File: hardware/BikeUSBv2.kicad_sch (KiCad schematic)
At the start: 52 parts, among them J1 TYPE-C-31-M-16, J2 JST S2B-EH(LF)(SN), SW1 1TS002E-2500-2501-CT, SW2 1TS002E-2500-2501-CT, U1 TPS63020DSJR, U2 ATtiny1616-M, U3 FUSB302B10MPX, U4 HT7550-2, U5 TPS25200

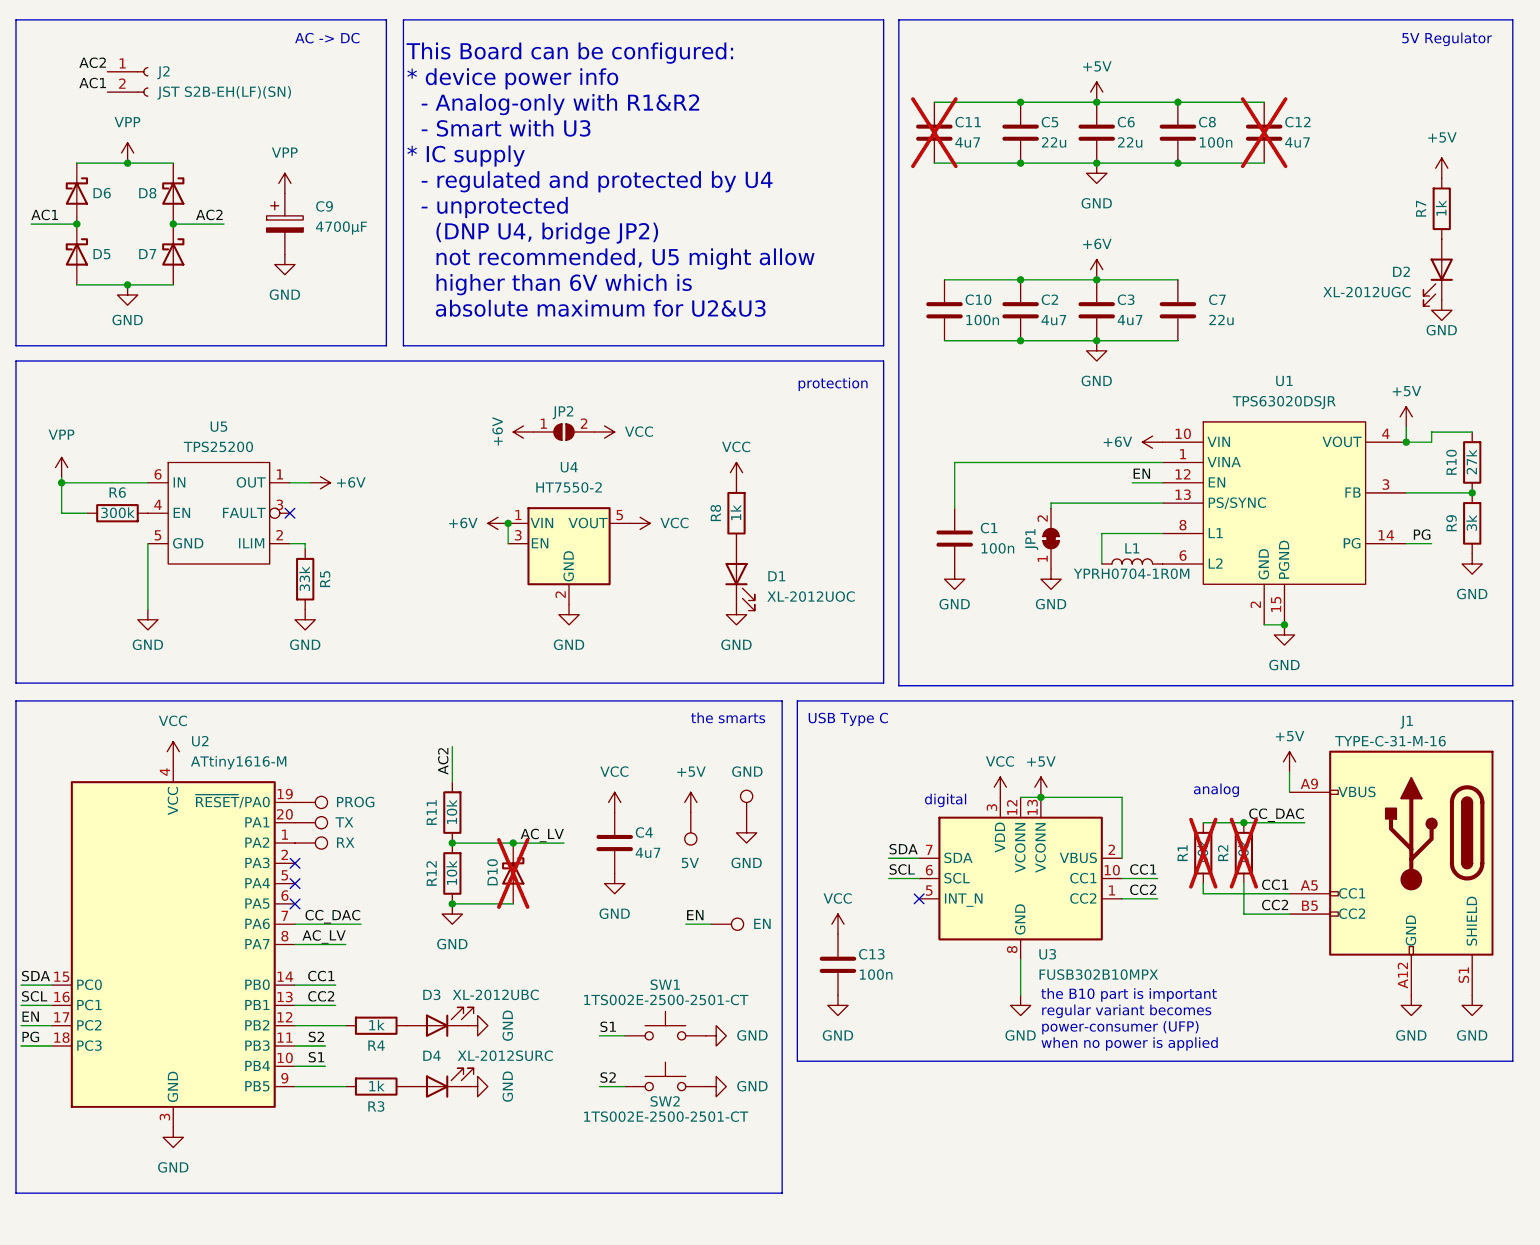
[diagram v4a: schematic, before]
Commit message: make U4 optional since new U5 clamps to 5V5
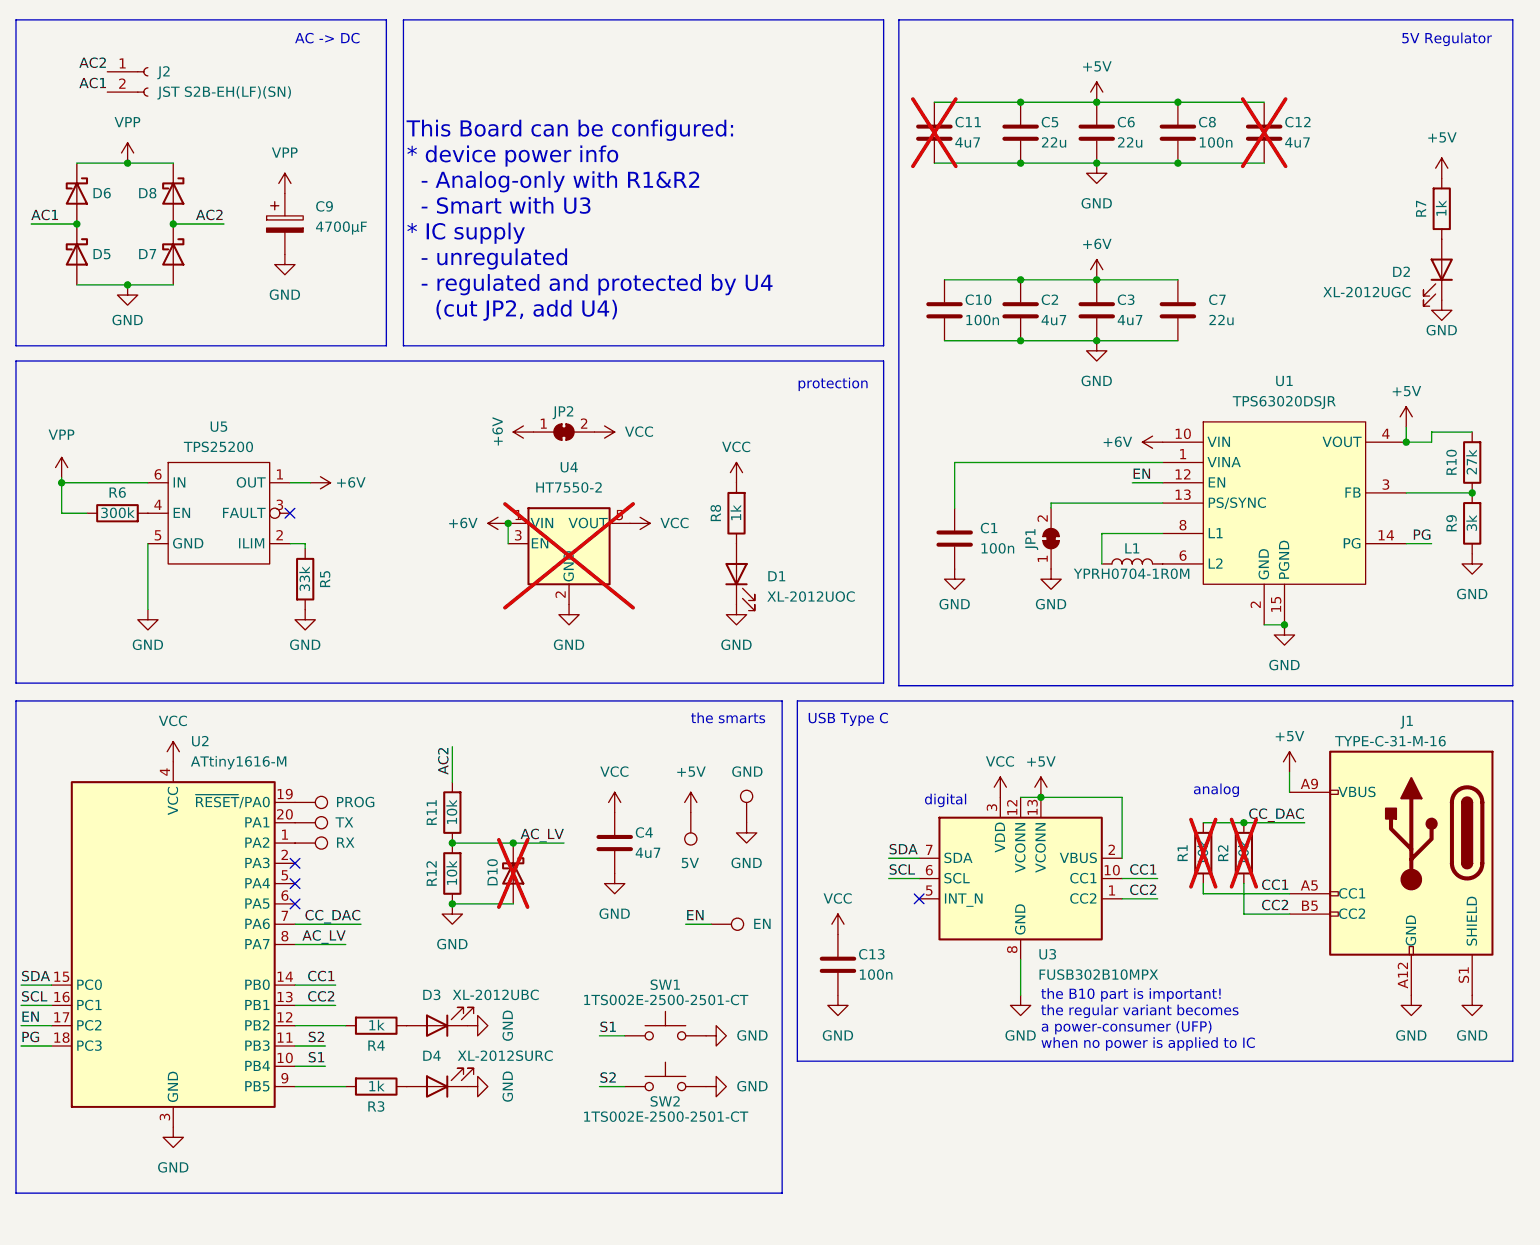
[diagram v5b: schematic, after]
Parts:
- JP2: footprint Jumper:SolderJumper-2_P1.3mm_Open_RoundedPad1.0x1.5mm -> Jumper:SolderJumper-2_P1.3mm_Bridged_RoundedPad1.0x1.5mm; symbol Jumper:SolderJumper_2_Open -> Jumper:SolderJumper_2_Bridged
- U4: now not fitted; now left out of the parts list
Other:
- note added: "This Board can be configured: * device power info - Analog-only with R1&R2 - Smart with U3 * IC supply - unregulated - regulated and protected by U4 (cut JP2, add U4)"
- note added: "the B10 part is important! the regular variant becomes a power-consumer (UFP) when no power is applied to IC"
- note removed: "This Board can be configured: * device power info - Analog-only with R1&R2 - Smart with U3 * IC supply - regulated and protected by U4 - unprotected (DNP U4, bridge JP2) not recommended, U5 might allow higher than 6V which is absolute maximum for U2&U3"
- note removed: "the B10 part is important regular variant becomes power-consumer (UFP) when no power is applied"
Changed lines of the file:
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@@
     (effects (font (size 1.27 1.27)) (justify left bottom))
   )
-  (text "the B10 part is important\nregular variant becomes\npower-consumer (UFP)\nwhen no power is applied"
+  (text "the B10 part is important!\nthe regular variant becomes\na power-consumer (UFP)\nwhen no power is applied to IC"
     (at 144.78 146.05 0)
     (effects (font (size 1.27 1.27)) (justify left bottom))
@@
     (effects (font (size 1.27 1.27)) (justify left bottom))
   )
-  (text "This Board can be configured:\n* device power info\n  - Analog-only with R1&R2\n  - Smart with U3\n* IC supply\n  - regulated and protected by U4\n  - unprotected\n    (DNP U4, bridge JP2)\n    not recommended, U5 might allow\n    higher than 6V which is\n    absolute maximum for U2&U3"
+  (text "This Board can be configured:\n* device power info\n  - Analog-only with R1&R2\n  - Smart with U3\n* IC supply\n  - unregulated\n  - regulated and protected by U4\n    (cut JP2, add U4)"
     (at 65.405 54.61 0)
     (effects (font (size 2 2)) (justify left bottom))
@@
     )
   )
-  (symbol (lib_id "Jumper:SolderJumper_2_Open") (at 85.09 68.58 0) (unit 1)
+  (symbol (lib_id "Jumper:SolderJumper_2_Bridged") (at 85.09 68.58 0) (unit 1)
     (in_bom no) (on_board yes) (dnp no)
     (property "Reference" "JP2" (at 85.09 66.04 0)
@@
       (effects (font (size 1.27 1.27)) hide)
     )
-    (property "Footprint" "Jumper:SolderJumper-2_P1.3mm_Open_RoundedPad1.0x1.5mm" (at 85.09 68.58 0)
+    (property "Footprint" "Jumper:SolderJumper-2_P1.3mm_Bridged_RoundedPad1.0x1.5mm" (at 85.09 68.58 0)
       (effects (font (size 1.27 1.27)) hide)
     )
@@
   )
   (symbol (lib_id "Regulator_Linear:AP2112K-3.3") (at 85.725 82.55 0) (unit 1)
-    (in_bom yes) (on_board yes) (dnp no) (fields_autoplaced)
+    (in_bom no) (on_board yes) (dnp yes) (fields_autoplaced)
     (property "Reference" "U4" (at 85.725 73.025 0)
       (effects (font (size 1.27 1.27)))

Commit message: cleanup
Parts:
- renumbered C9 to C0, C2 to C1, C4 to C10, C5 to C11, C11 to C12, C3 to C2, C7 to C3, C10 to C4, C1 to C5, C8 to C6, C12 to C7, C6 to C8, C13 to C9, JP2 to JP1, JP1 to JP2, R6 to R1, R1 to R10, R2 to R11, R4 to R12, R5 to R2, R10 to R3, R9 to R4, R7 to R5, R11 to R6, R12 to R7, R3 to R9, SW2 to SW1, SW1 to SW2, TP7 to TP1, TP6 to TP2, TP2 to TP3, TP1 to TP4, TP4 to TP5, TP5 to TP6

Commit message: stuff
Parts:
- renumbered SW2 to SW1, SW1 to SW2
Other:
- note added: "This Board can be configured: * device power info - Analog-only with R10&R11 - Smart with U3 * IC supply - unregulated - regulated and protected by U4 (cut JP2, add U4)"
- note removed: "This Board can be configured: * device power info - Analog-only with R1&R2 - Smart with U3 * IC supply - unregulated - regulated and protected by U4 (cut JP2, add U4)"
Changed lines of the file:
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@@
     (effects (font (size 1.27 1.27)) (justify left bottom))
   )
-  (text "This Board can be configured:\n* device power info\n  - Analog-only with R1&R2\n  - Smart with U3\n* IC supply\n  - unregulated\n  - regulated and protected by U4\n    (cut JP2, add U4)"
+  (text "This Board can be configured:\n* device power info\n  - Analog-only with R10&R11\n  - Smart with U3\n* IC supply\n  - unregulated\n  - regulated and protected by U4\n    (cut JP2, add U4)"
     (at 65.405 54.61 0)
     (effects (font (size 2 2)) (justify left bottom))
@@
   (symbol (lib_id "Switch:SW_Push") (at 97.79 150.495 0) (unit 1)
     (in_bom yes) (on_board yes) (dnp no)
-    (property "Reference" "SW1" (at 97.79 152.4 0)
+    (property "Reference" "SW2" (at 97.79 152.4 0)
       (effects (font (size 1.27 1.27)))
     )
@@
       (project "BikeUSBv2"
         (path "/b4aff538-5116-4944-9d24-c26a88d7dfe8"
-          (reference "SW1") (unit 1)
+          (reference "SW2") (unit 1)
         )
       )
@@
   (symbol (lib_id "Switch:SW_Push") (at 97.79 144.145 0) (unit 1)
     (in_bom yes) (on_board yes) (dnp no)
-    (property "Reference" "SW2" (at 97.79 137.795 0)
+    (property "Reference" "SW1" (at 97.79 137.795 0)
       (effects (font (size 1.27 1.27)))
     )
@@
       (project "BikeUSBv2"
         (path "/b4aff538-5116-4944-9d24-c26a88d7dfe8"
-          (reference "SW2") (unit 1)
-        )
-      )
+          (reference "SW1") (unit 1)
+        )
+      )

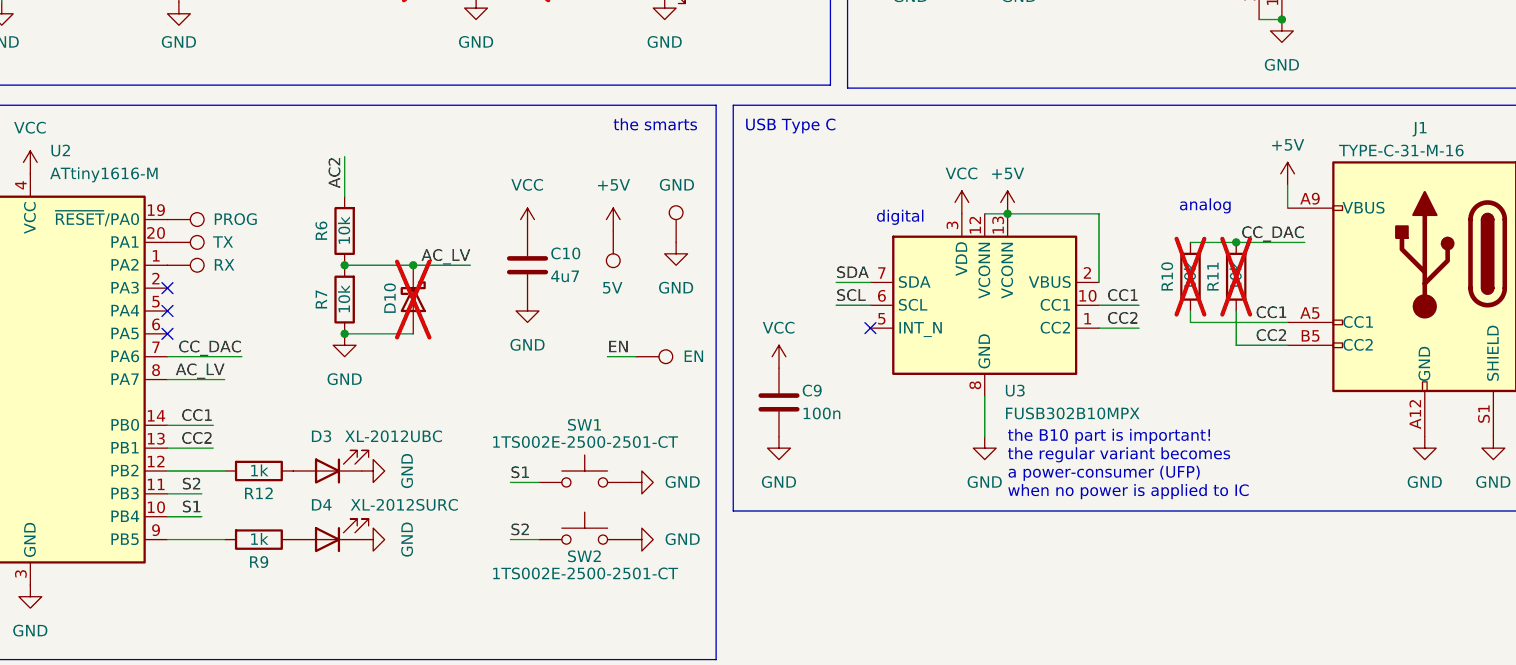
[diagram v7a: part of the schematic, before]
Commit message: add INT line between U3 and U2
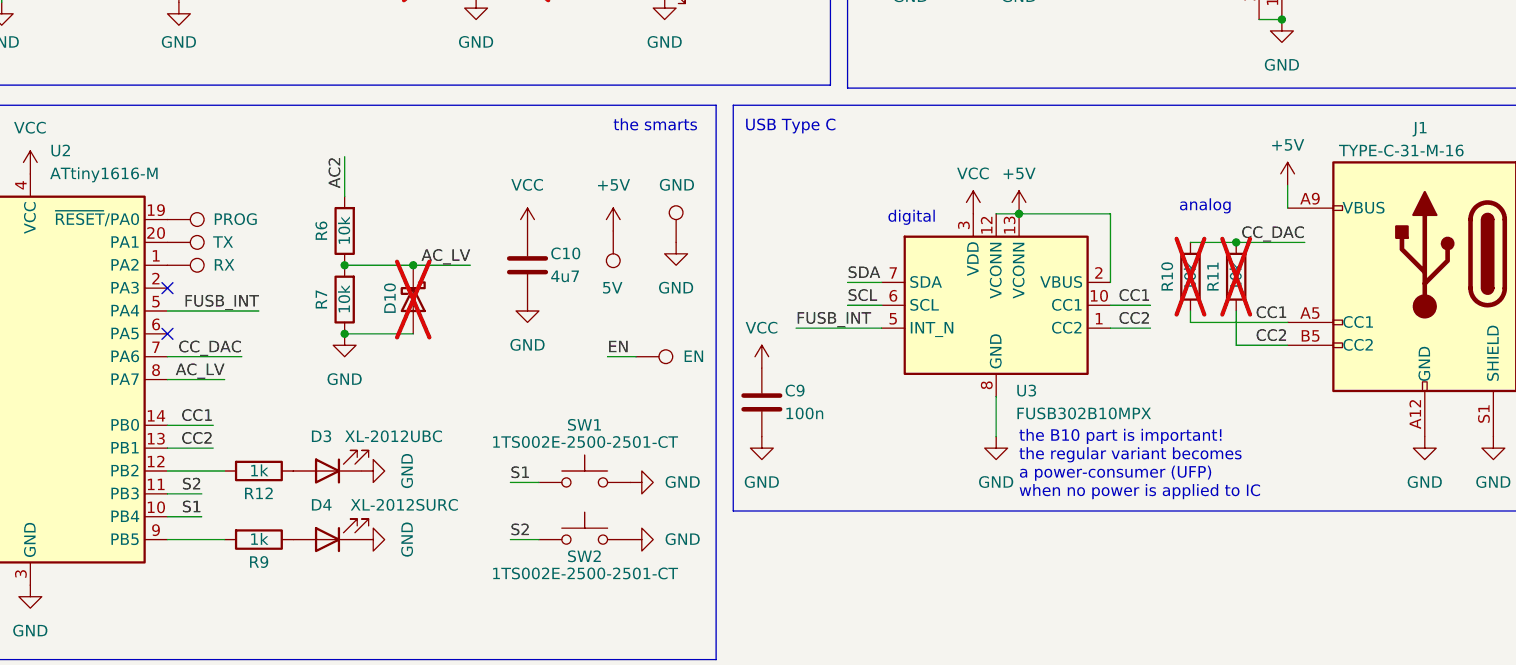
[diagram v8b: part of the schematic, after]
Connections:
- net FUSB_INT: now reaches U2.5 (PA4)
- net FUSB_INT: now also U3.5 (INT_N)
- no-connect marks 5 -> 3
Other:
- moved on the sheet: C9, U3
